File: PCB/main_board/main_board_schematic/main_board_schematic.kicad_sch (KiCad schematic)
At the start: 256 parts, among them J1 Conn_01x02, J2 Conn_01x02, J3 Conn_01x02, P1 USB_C_Plug_USB2.0, U1 NCP1117-3.3_SOT223, U2 RP2040, U3 W25Q128JVS, Y1 12MHZ

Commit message: Connected matrix to the rp2040
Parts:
- J1, J2, J3: footprint Connector_PinHeader_2.54mm:PinHeader_1x02_P2.54mm_Horizontal -> Connector_PinHeader_2.54mm:PinHeader_1x02_P2.54mm_Vertical
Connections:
- net GPIO0 is gone; now on net GND: U2.2 (GPIO0)
- net GPIO1 is gone; now on net GND: U2.3 (GPIO1)
- net GPIO10 is gone; now on net GND: U2.13 (GPIO10)
- net GPIO8 is gone; now on net GND: U2.11 (GPIO8)
- net GPIO9 is gone; now on net GND: U2.12 (GPIO9)
- net IN0 is gone; now on net GPIO12: D1.2 (A), D10.2 (A), D108.2 (A), D20.2 (A), D30.2 (A), D40.2 (A), D50.2 (A), D64.2 (A), D75.2 (A), D86.2 (A), D93.2 (A), D99.2 (A)
- net IN1 is gone; now on net GPIO13: D11.2 (A), D21.2 (A), D31.2 (A), D41.2 (A), D51.2 (A), D63.2 (A), D74.2 (A), D85.2 (A), D92.2 (A), D98.2 (A)
- net IN10 is gone; now on net GPIO11: D100.2 (A), D65.2 (A), D76.2 (A), D87.2 (A)
- net IN2 is gone; now on net GPIO14: D107.2 (A), D12.2 (A), D2.2 (A), D22.2 (A), D32.2 (A), D42.2 (A), D52.2 (A), D62.2 (A), D73.2 (A), D84.2 (A), D91.2 (A), D97.2 (A)
- net IN3 is gone; now on net GPIO15: D106.2 (A), D13.2 (A), D23.2 (A), D3.2 (A), D33.2 (A), D43.2 (A), D61.2 (A), D72.2 (A), D83.2 (A)
- net IN4 is gone; now on net GPIO16: D105.2 (A), D14.2 (A), D24.2 (A), D34.2 (A), D4.2 (A), D44.2 (A), D60.2 (A), D71.2 (A), D82.2 (A), D96.2 (A)
- net IN5 is gone; now on net GPIO17: D104.2 (A), D15.2 (A), D25.2 (A), D35.2 (A), D45.2 (A), D5.2 (A), D53.2 (A), D59.2 (A), D70.2 (A), D81.2 (A)
- net IN6 is gone; now on net GPIO21: D103.2 (A), D16.2 (A), D26.2 (A), D36.2 (A), D46.2 (A), D58.2 (A), D6.2 (A), D69.2 (A), D80.2 (A), D90.2 (A), D95.2 (A)
- net IN7 is gone; now on net GPIO20: D17.2 (A), D27.2 (A), D37.2 (A), D47.2 (A), D57.2 (A), D68.2 (A), D7.2 (A), D79.2 (A)
- net IN8 is gone; now on net GPIO19: D102.2 (A), D18.2 (A), D28.2 (A), D38.2 (A), D48.2 (A), D56.2 (A), D67.2 (A), D78.2 (A), D8.2 (A), D89.2 (A)
- net IN9 is gone; now on net GPIO18: D101.2 (A), D19.2 (A), D29.2 (A), D39.2 (A), D49.2 (A), D54.2 (A), D55.2 (A), D66.2 (A), D77.2 (A), D88.2 (A), D9.2 (A), D94.2 (A)
- net OUT0 is gone; now on net GPIO28: MX1.2, MX2.2, MX3.2, MX4.2, MX5.2, MX6.2, MX7.2, MX8.2, MX9.2
- net OUT1 is gone; now on net GPIO27: MX10.2, MX11.2, MX12.2, MX13.2, MX14.2, MX15.2, MX16.2, MX17.2, MX18.2, MX19.2
- net OUT10 is gone; now on net GPIO6: MX100.2, MX94.2, MX95.2, MX96.2, MX97.2, MX98.2, MX99.2
- net OUT11 is gone; now on net GPIO7: MX101.2, MX102.2, MX103.2, MX104.2, MX105.2, MX106.2, MX107.2, MX108.2
- net OUT2 is gone; now on net GPIO26: MX20.2, MX21.2, MX22.2, MX23.2, MX24.2, MX25.2, MX26.2, MX27.2, MX28.2, MX29.2
- net OUT3 is gone; now on net GPIO24: MX30.2, MX31.2, MX32.2, MX33.2, MX34.2, MX35.2, MX36.2, MX37.2, MX38.2, MX39.2
- net OUT4 is gone; now on net GPIO23: MX40.2, MX41.2, MX42.2, MX43.2, MX44.2, MX45.2, MX46.2, MX47.2, MX48.2, MX49.2
- net OUT5 is gone; now on net GPIO22: MX50.2, MX51.2, MX52.2, MX53.2, MX54.2
- net OUT6 is gone; now on net GPIO2: MX55.2, MX56.2, MX57.2, MX58.2, MX59.2, MX60.2, MX61.2, MX62.2, MX63.2, MX64.2, MX65.2
- net OUT7 is gone; now on net GPIO3: MX66.2, MX67.2, MX68.2, MX69.2, MX70.2, MX71.2, MX72.2, MX73.2, MX74.2, MX75.2, MX76.2
- net OUT8 is gone; now on net GPIO4: MX77.2, MX78.2, MX79.2, MX80.2, MX81.2, MX82.2, MX83.2, MX84.2, MX85.2, MX86.2, MX87.2
- net OUT9 is gone; now on net GPIO5: MX88.2, MX89.2, MX90.2, MX91.2, MX92.2, MX93.2

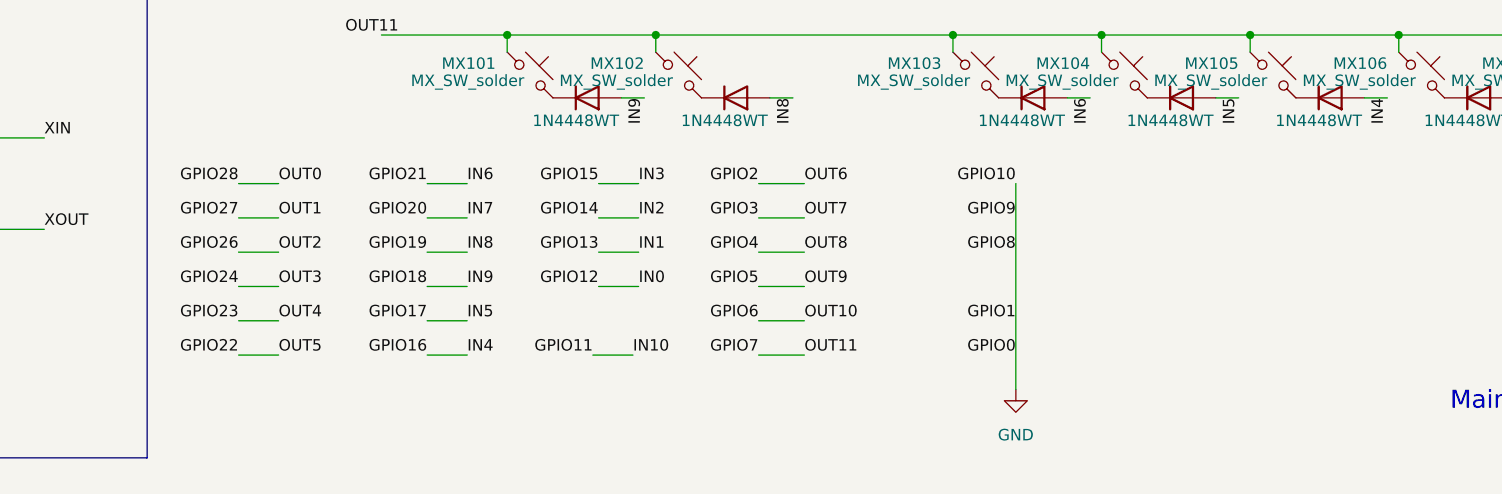
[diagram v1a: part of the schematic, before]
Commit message: Moved usb-c connector and added labels
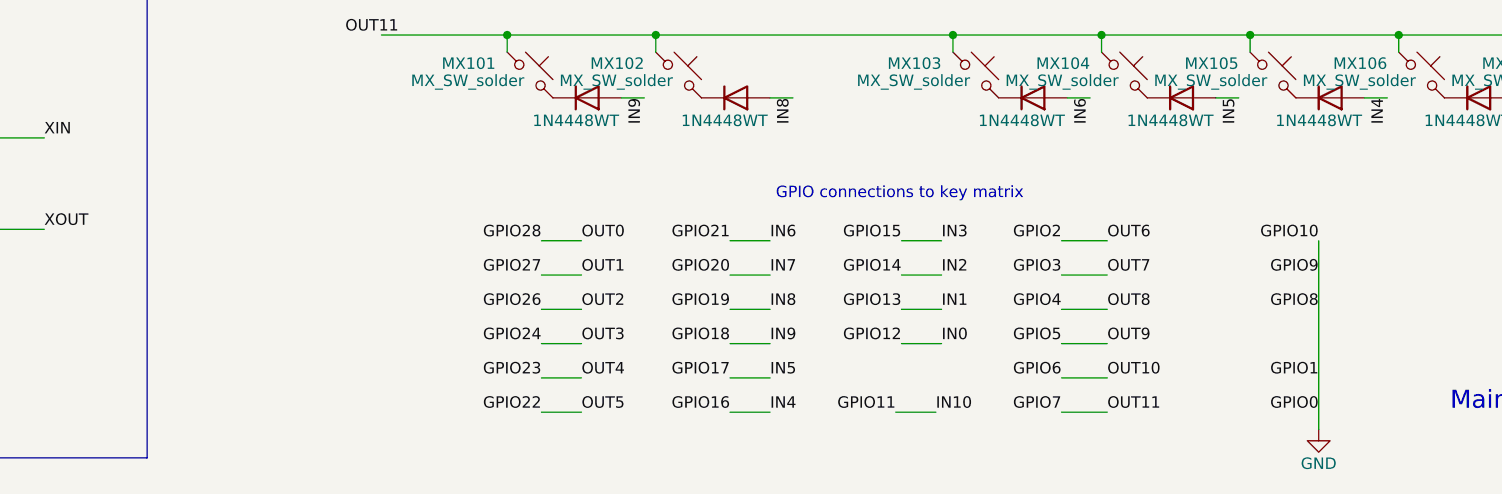
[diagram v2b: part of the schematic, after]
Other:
- note added: "GPIO connections to key matrix"

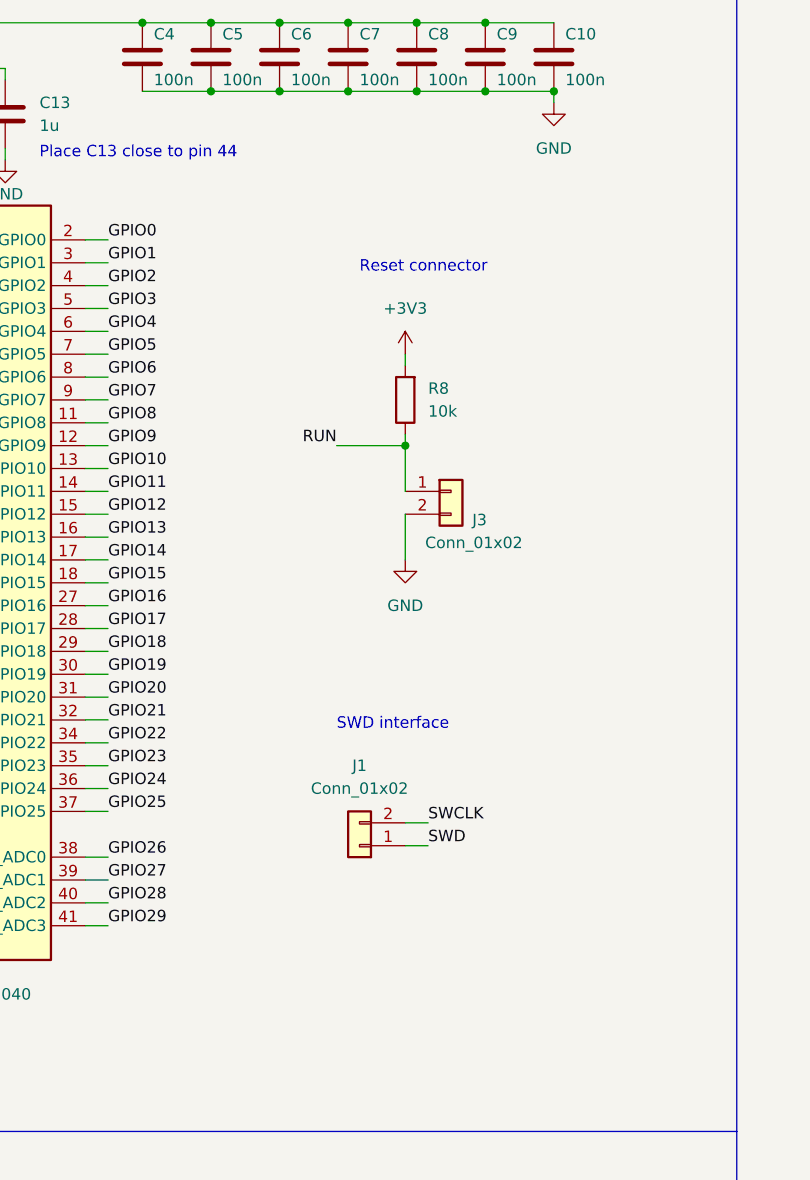
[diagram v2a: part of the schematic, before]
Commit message: Added a led connected to pin25
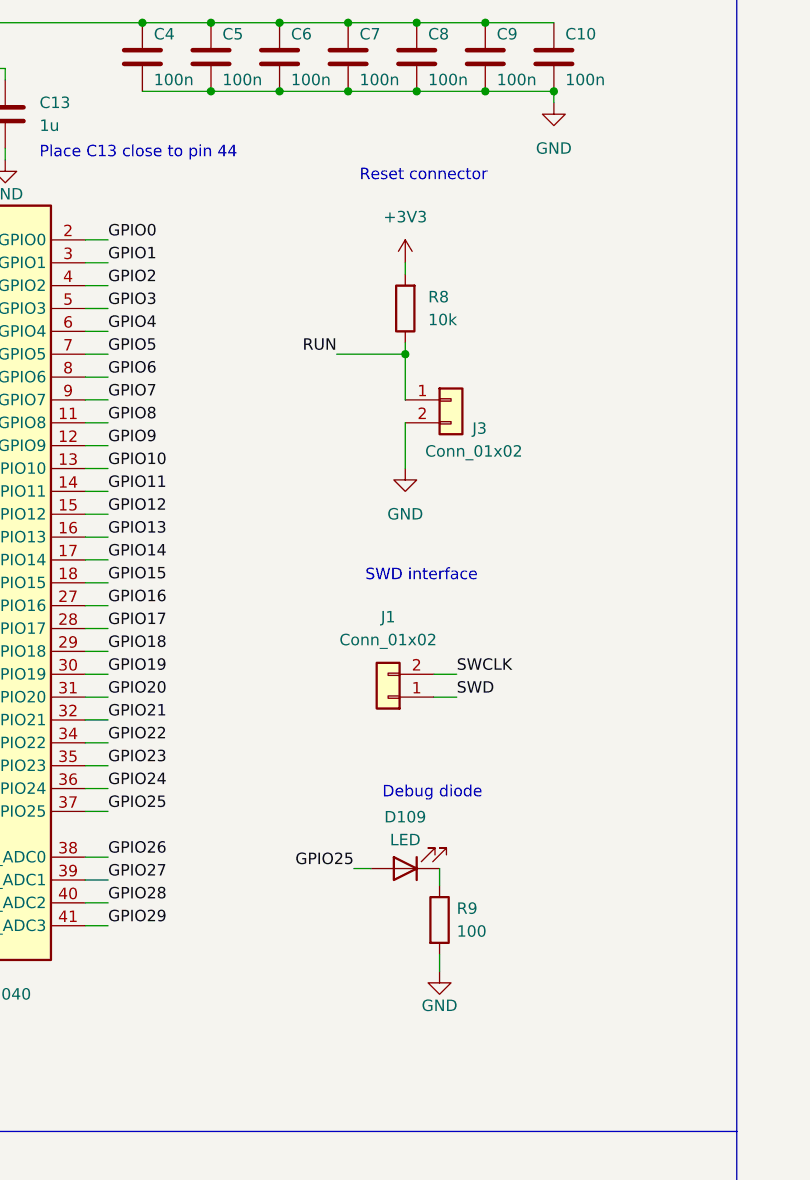
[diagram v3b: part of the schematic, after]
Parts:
- added D109: LED, LED_SMD:LED_0603_1608Metric, symbol Device:LED
- added R9: 100, Resistor_SMD:R_0603_1608Metric, symbol Device:R
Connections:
- net GND: now also R9.2
- net GPIO25: now also D109.2 (A)
- new net: D109.1 (K), R9.1
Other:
- note added: "Debug diode"
- moved on the sheet: J1, J3, R8

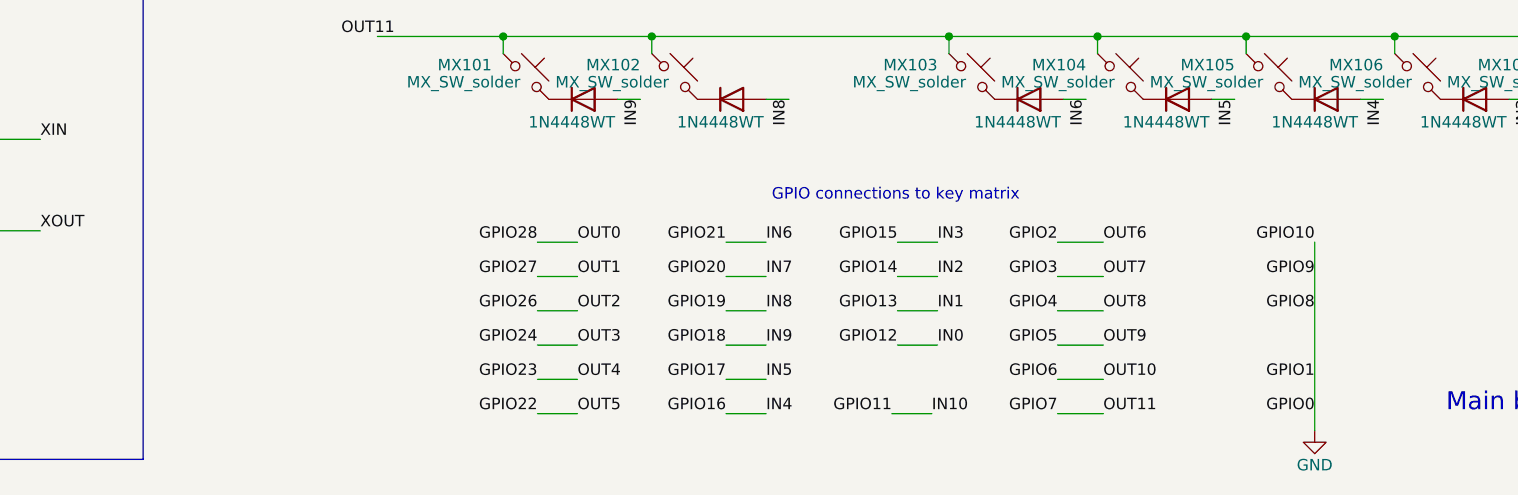
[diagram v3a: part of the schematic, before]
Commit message: Exposed pins and power rails
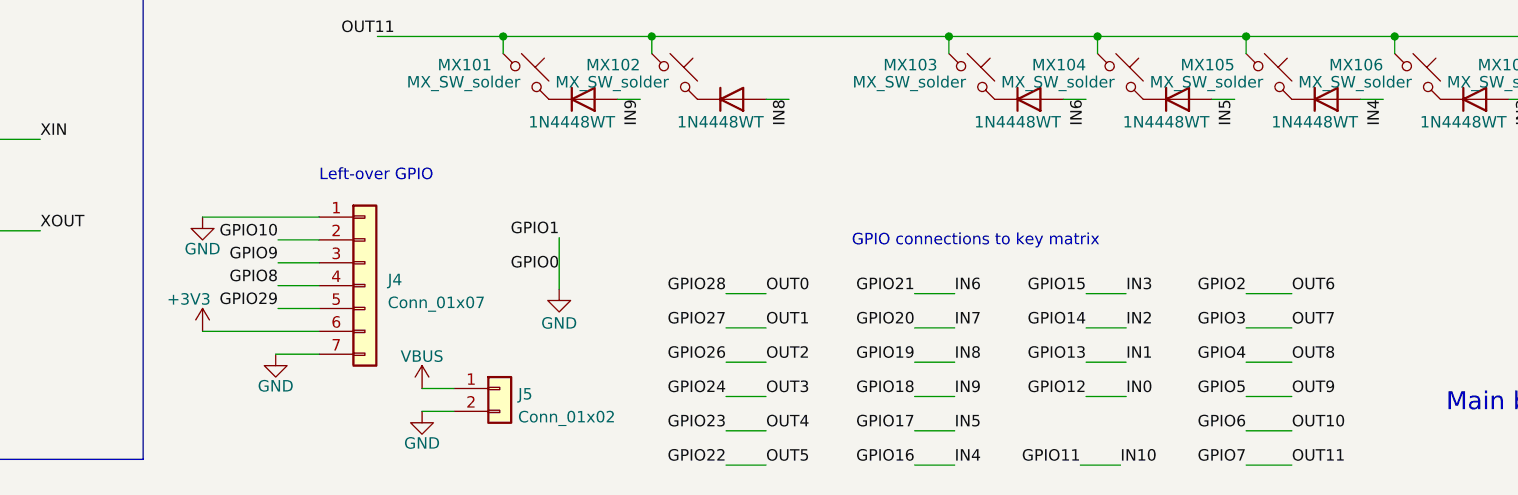
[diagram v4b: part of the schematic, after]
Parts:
- added J4: Conn_01x07, Connector_PinSocket_2.54mm:PinSocket_1x07_P2.54mm_Vertical, symbol Connector_Generic:Conn_01x07
- added J5: Conn_01x02, Connector_PinSocket_2.54mm:PinSocket_1x02_P2.54mm_Vertical, symbol Connector_Generic:Conn_01x02
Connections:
- net +3V3: now also J4.6 (Pin_6)
- net GND: now also J4.1 (Pin_1), J4.7 (Pin_7), J5.2 (Pin_2); no longer U2.11 (GPIO8), U2.12 (GPIO9), U2.13 (GPIO10)
- net GPIO29: now also J4.5 (Pin_5)
- net VBUS: now also J5.1 (Pin_1)
- new net GPIO10: J4.2 (Pin_2), U2.13 (GPIO10)
- new net GPIO8: J4.4 (Pin_4), U2.11 (GPIO8)
- new net GPIO9: J4.3 (Pin_3), U2.12 (GPIO9)
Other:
- note added: "Left-over GPIO"

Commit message: Fixed footprints for pins
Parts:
- J4: footprint Connector_PinSocket_2.54mm:PinSocket_1x07_P2.54mm_Vertical -> Connector_PinHeader_2.54mm:PinHeader_1x07_P2.54mm_Vertical
- J5: footprint Connector_PinSocket_2.54mm:PinSocket_1x02_P2.54mm_Vertical -> Connector_PinHeader_2.54mm:PinHeader_1x02_P2.54mm_Vertical
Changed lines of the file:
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@@
       (effects (font (size 1.27 1.27)) (justify left))
     )
-    (property "Footprint" "Connector_PinSocket_2.54mm:PinSocket_1x02_P2.54mm_Vertical" (at 204.724 275.336 0)
+    (property "Footprint" "Connector_PinHeader_2.54mm:PinHeader_1x02_P2.54mm_Vertical" (at 204.724 275.336 0)
       (effects (font (size 1.27 1.27)) hide)
     )
@@
       (effects (font (size 1.27 1.27)) (justify left))
     )
-    (property "Footprint" "Connector_PinSocket_2.54mm:PinSocket_1x07_P2.54mm_Vertical" (at 189.738 263.906 0)
-      (effects (font (size 1.27 1.27)) hide)
-    )
+    (property "Footprint" "Connector_PinHeader_2.54mm:PinHeader_1x07_P2.54mm_Vertical" (at 189.738 263.906 0)
+      (effects (font (size 1.27 1.27)) hide)
+    )
